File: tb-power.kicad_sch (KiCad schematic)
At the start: 56 parts, among them Q1 BC817-25W, U4 JHL6340SLLSQ

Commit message: Run kmake loclib
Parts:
- C51, C52, C53, C54, C55, C56, C57, C58, C59, C60, C61, C62, C63, C64, C65, C66, C67, C68, C69, C71, C72, C73, C74, C77, C81, C84, C85, C87, C90, C94: footprint antmicro-footprints:C_0402_1005Metric -> thunderbolt-adapter-footprints:C_0402_1005Metric; symbol antmicroCapacitors0402:C_1u_0402 -> thunderbolt-adapter:C_1u_0402
- C70, C75, C76, C78, C80, C83, C96: footprint antmicro-footprints:C_0402_1005Metric -> thunderbolt-adapter-footprints:C_0402_1005Metric; symbol antmicroCapacitors0402:C_10u_0402 -> thunderbolt-adapter:C_10u_0402
- C79, C82, C86, C89: footprint antmicro-footprints:C_0603_1608Metric -> thunderbolt-adapter-footprints:C_0603_1608Metric; symbol antmicroCapacitors0603:C_22u_0603 -> thunderbolt-adapter:C_22u_0603
- C88, C91, C92, C93, C95, C97: footprint antmicro-footprints:C_0402_1005Metric -> thunderbolt-adapter-footprints:C_0402_1005Metric; symbol antmicroCapacitors0402:C_100n_0402 -> thunderbolt-adapter:C_100n_0402
- D4: footprint antmicro-footprints:LED_0603_1608Metric_G -> thunderbolt-adapter-footprints:LED_0603_1608Metric_G; symbol antmicroLEDIndicationDiscrete:LED_G_0603_KP-1608CGCK -> thunderbolt-adapter:LED_G_0603_KP-1608CGCK
- L3: footprint antmicro-footprints:L_Vishay-IHLP1616BZ -> thunderbolt-adapter-footprints:L_Vishay-IHLP1616BZ; symbol antmicroFixedInductors:L_680n_7.6A_IHLP1616BZ -> thunderbolt-adapter:L_680n_7.6A_IHLP1616BZ
- L4: footprint antmicro-footprints:L_0603_1608Metric -> thunderbolt-adapter-footprints:L_0603_1608Metric; symbol antmicroFixedInductors:L_1u_1.8A_0603 -> thunderbolt-adapter:L_1u_1.8A_0603
- Q1: footprint antmicro-footprints:SOT-323 -> thunderbolt-adapter-footprints:SOT-323; symbol antmicroTransistorsBipolarSingle:BC817-25W -> thunderbolt-adapter:BC817-25W
- R47: footprint antmicro-footprints:R_0402_1005Metric -> thunderbolt-adapter-footprints:R_0402_1005Metric; symbol antmicroResistors0402:R_1k_0402 -> thunderbolt-adapter:R_1k_0402
- R48: footprint antmicro-footprints:R_0402_1005Metric -> thunderbolt-adapter-footprints:R_0402_1005Metric; symbol antmicroResistors0402:R_100k_0402 -> thunderbolt-adapter:R_100k_0402
- R49: footprint antmicro-footprints:R_0402_1005Metric -> thunderbolt-adapter-footprints:R_0402_1005Metric; symbol antmicroResistors0402:R_330R_0402 -> thunderbolt-adapter:R_330R_0402
- TP9: footprint antmicro-footprints:Testpoint_smd_1mm -> thunderbolt-adapter-footprints:Testpoint_smd_1mm; symbol antmicroTestPoints:TP_1mm_SMD -> thunderbolt-adapter:TP_1mm_SMD
- U4: footprint antmicro-footprints:JHL6340SLLSQ -> thunderbolt-adapter-footprints:JHL6340SLLSQ; symbol antmicroInterfaceControllers:JHL6340SLLSQ -> thunderbolt-adapter:JHL6340SLLSQ

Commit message: Rename project to thunderbolt-gpu-adapter
Fix Amphenol 10146070-113Y0LF footprint
Add missing 3D models, update selected footprints
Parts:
- C51, C52, C53, C54, C55, C56, C57, C58, C59, C60, C61, C62, C63, C64, C65, C66, C67, C68, C69, C71, C72, C73, C74, C77, C81, C84, C85, C87, C90, C94: footprint thunderbolt-adapter-footprints:C_0402_1005Metric -> thunderbolt-gpu-adapter-footprints:C_0402_1005Metric; symbol thunderbolt-adapter:C_1u_0402 -> thunderbolt-gpu-adapter:C_1u_0402
- C70, C75, C76, C78, C80, C83, C96: footprint thunderbolt-adapter-footprints:C_0402_1005Metric -> thunderbolt-gpu-adapter-footprints:C_0402_1005Metric; symbol thunderbolt-adapter:C_10u_0402 -> thunderbolt-gpu-adapter:C_10u_0402
- C79, C82, C86, C89: footprint thunderbolt-adapter-footprints:C_0603_1608Metric -> thunderbolt-gpu-adapter-footprints:C_0603_1608Metric; symbol thunderbolt-adapter:C_22u_0603 -> thunderbolt-gpu-adapter:C_22u_0603
- C88, C91, C92, C93, C95, C97: footprint thunderbolt-adapter-footprints:C_0402_1005Metric -> thunderbolt-gpu-adapter-footprints:C_0402_1005Metric; symbol thunderbolt-adapter:C_100n_0402 -> thunderbolt-gpu-adapter:C_100n_0402
- D4: footprint thunderbolt-adapter-footprints:LED_0603_1608Metric_G -> thunderbolt-gpu-adapter-footprints:LED_0603_1608Metric_G; symbol thunderbolt-adapter:LED_G_0603_KP-1608CGCK -> thunderbolt-gpu-adapter:LED_G_0603_KP-1608CGCK
- L3: footprint thunderbolt-adapter-footprints:L_Vishay-IHLP1616BZ -> thunderbolt-gpu-adapter-footprints:L_Vishay-IHLP1616BZ; symbol thunderbolt-adapter:L_680n_7.6A_IHLP1616BZ -> thunderbolt-gpu-adapter:L_680n_7.6A_IHLP1616BZ
- L4: footprint thunderbolt-adapter-footprints:L_0603_1608Metric -> thunderbolt-gpu-adapter-footprints:L_0603_1608Metric; symbol thunderbolt-adapter:L_1u_1.8A_0603 -> thunderbolt-gpu-adapter:L_1u_1.8A_0603
- Q1: footprint thunderbolt-adapter-footprints:SOT-323 -> thunderbolt-gpu-adapter-footprints:SOT-323; symbol thunderbolt-adapter:BC817-25W -> thunderbolt-gpu-adapter:BC817-25W
- R47: footprint thunderbolt-adapter-footprints:R_0402_1005Metric -> thunderbolt-gpu-adapter-footprints:R_0402_1005Metric; symbol thunderbolt-adapter:R_1k_0402 -> thunderbolt-gpu-adapter:R_1k_0402
- R48: footprint thunderbolt-adapter-footprints:R_0402_1005Metric -> thunderbolt-gpu-adapter-footprints:R_0402_1005Metric; symbol thunderbolt-adapter:R_100k_0402 -> thunderbolt-gpu-adapter:R_100k_0402
- R49: footprint thunderbolt-adapter-footprints:R_0402_1005Metric -> thunderbolt-gpu-adapter-footprints:R_0402_1005Metric; symbol thunderbolt-adapter:R_330R_0402 -> thunderbolt-gpu-adapter:R_330R_0402
- TP9: footprint thunderbolt-adapter-footprints:Testpoint_smd_1mm -> thunderbolt-gpu-adapter-footprints:Testpoint_smd_1mm; symbol thunderbolt-adapter:TP_1mm_SMD -> thunderbolt-gpu-adapter:TP_1mm_SMD
- U4: footprint thunderbolt-adapter-footprints:JHL6340SLLSQ -> thunderbolt-gpu-adapter-footprints:JHL6340SLLSQ; symbol thunderbolt-adapter:JHL6340SLLSQ -> thunderbolt-gpu-adapter:JHL6340SLLSQ

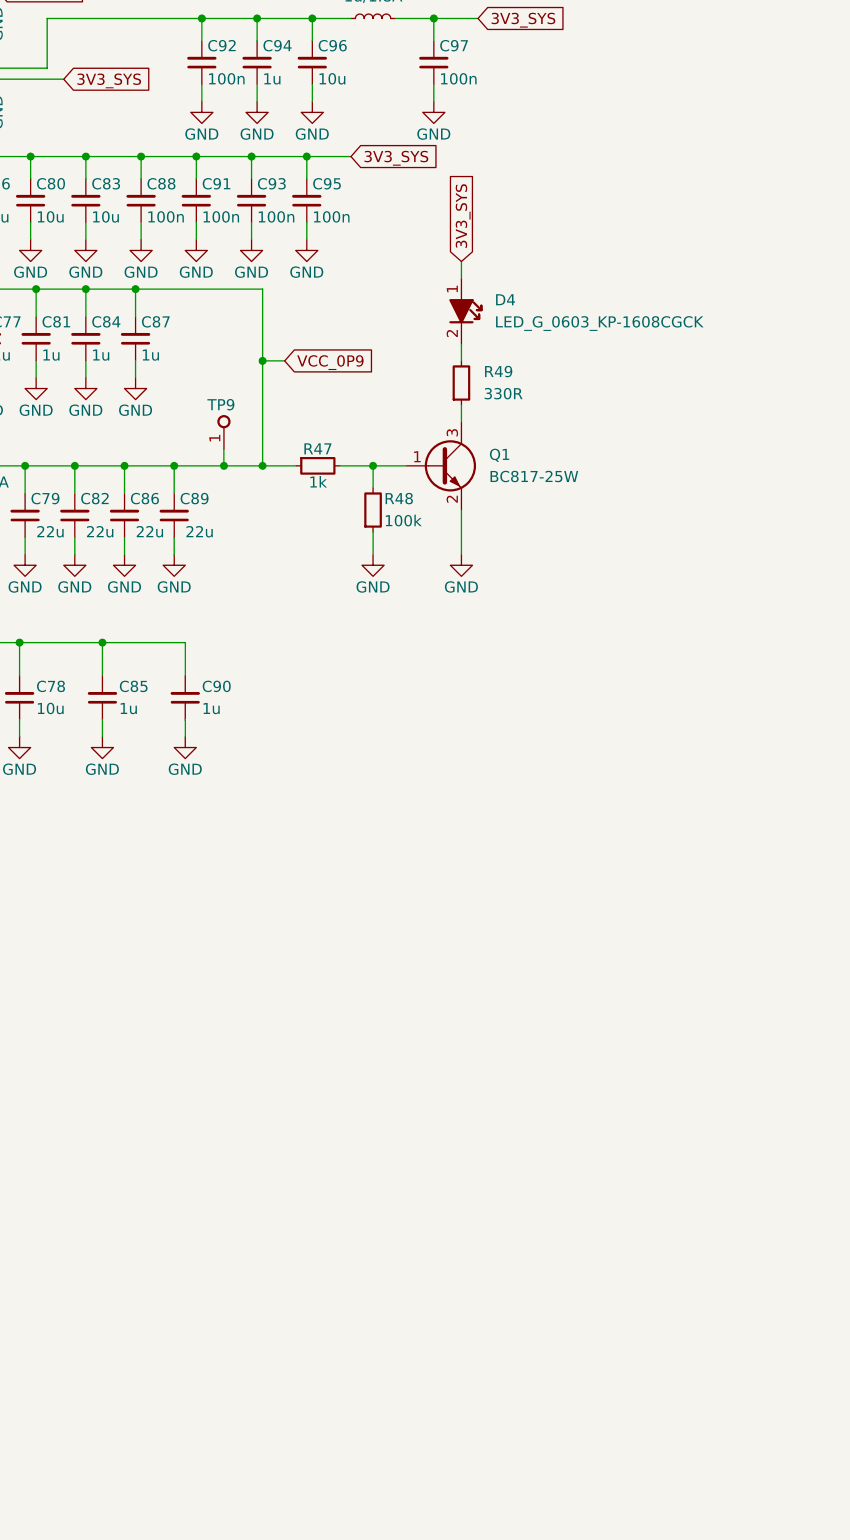
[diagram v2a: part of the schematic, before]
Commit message: Update PCIe power switching circuit (SCH)
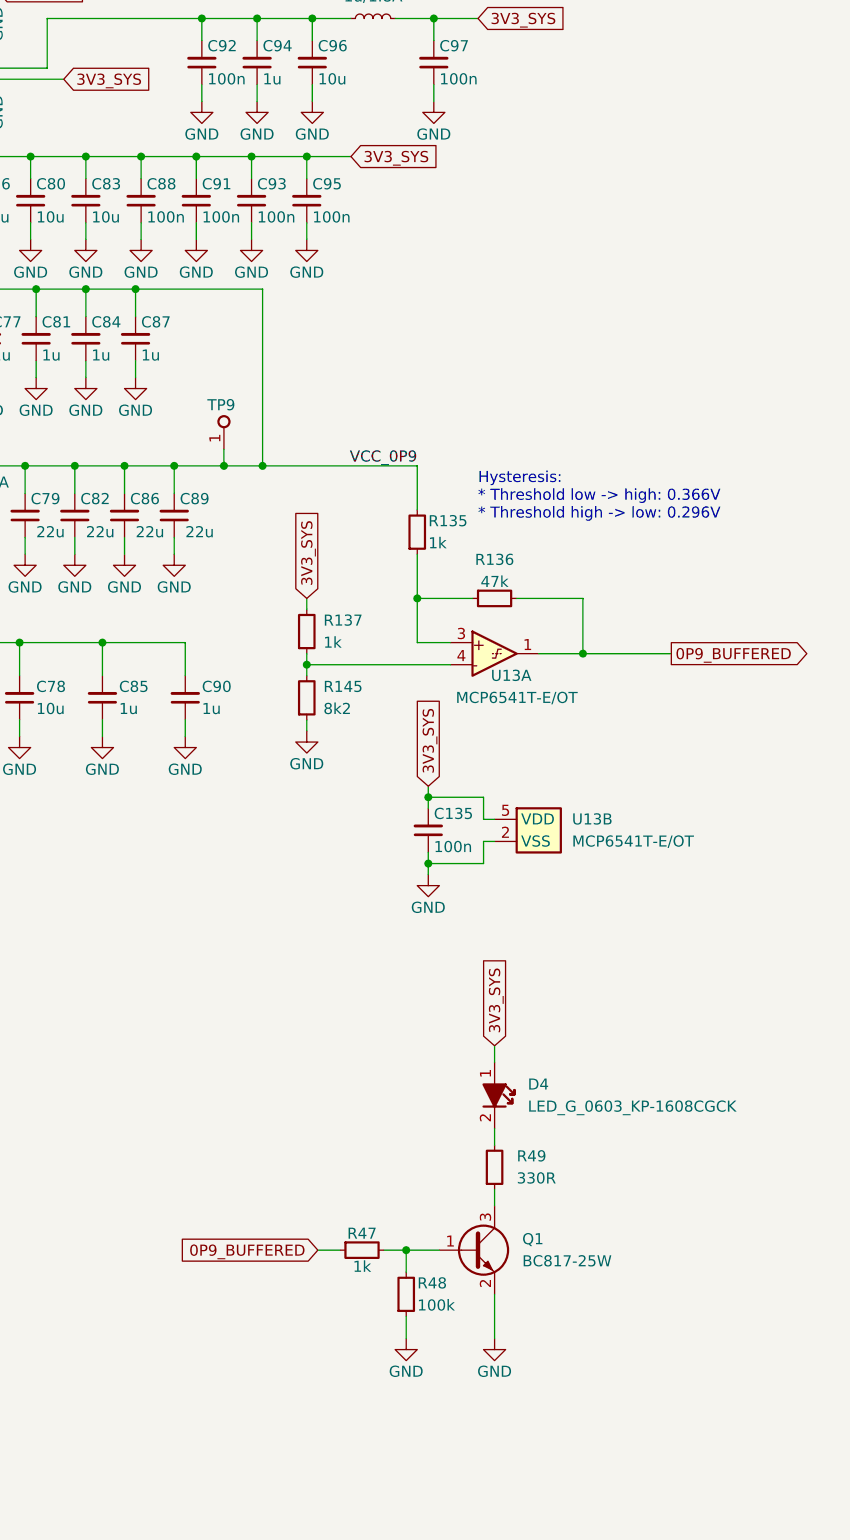
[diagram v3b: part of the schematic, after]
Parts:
- added C135: C_100n_0402, thunderbolt-gpu-adapter-footprints:C_0402_1005Metric, symbol thunderbolt-gpu-adapter:C_100n_0402
- added R135, R137: R_1k_0402, antmicro-footprints:R_0402_1005Metric, symbol antmicroResistors0402:R_1k_0402
- added R136: R_47k_0402, antmicro-footprints:R_0402_1005Metric, symbol antmicroResistors0402:R_47k_0402
- added R145: R_8k2_0402, antmicro-footprints:R_0402_1005Metric, symbol antmicroResistors0402:R_8k2_0402
- added U13: MCP6541_SOT23-5_Split, antmicro-footprints:SOT-23-5, symbol antmicroOperationalAmplifiers:MCP6541_SOT23-5_Split
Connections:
- net 3V3_SYS: now also C135.2, R137.2, U13.5 (VDD)
- net GND: now also C135.1, R145.1, U13.2 (VSS)
- net VCC_0P9: now also R135.2; no longer R47.1
- new net: R135.1, R136.1, U13.3
- new net: R137.1, R145.2, U13.4
- new net 0P9_BUFFERED: R136.2, R47.1, U13.1
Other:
- note added: "Hysteresis: * Threshold low -> high: 0.366V * Threshold high -> low: 0.296V"
- moved on the sheet: D4, Q1, R47, R48, R49

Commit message: Fix PCIe power switch - layout, bump revision to 1.1.2
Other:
- company: (none) -> Antmicro Ltd
- title: (none) -> Thunderbolt GPU Adapter
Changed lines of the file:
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@@
   (paper "A3" portrait)
   (title_block
-    (date "2023-05-09")
-    (rev "1.1.1")
+    (title "Thunderbolt GPU Adapter")
+    (date "2023-11-21")
+    (rev "1.1.2")
+    (company "Antmicro Ltd")
     (comment 1 "www.antmicro.com")
-    (comment 2 "Antmicro Ltd.")
   )
   (junction (at 116.205 80.01) (diameter 0) (color 0 0 0 0)

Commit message: Run kmake loclib
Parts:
- R135, R137: footprint antmicro-footprints:R_0402_1005Metric -> thunderbolt-gpu-adapter-footprints:R_0402_1005Metric; symbol antmicroResistors0402:R_1k_0402 -> thunderbolt-gpu-adapter:R_1k_0402
- R136: footprint antmicro-footprints:R_0402_1005Metric -> thunderbolt-gpu-adapter-footprints:R_0402_1005Metric; symbol antmicroResistors0402:R_47k_0402 -> thunderbolt-gpu-adapter:R_47k_0402
- R145: footprint antmicro-footprints:R_0402_1005Metric -> thunderbolt-gpu-adapter-footprints:R_0402_1005Metric; symbol antmicroResistors0402:R_8k2_0402 -> thunderbolt-gpu-adapter:R_8k2_0402
- U13: footprint antmicro-footprints:SOT-23-5 -> thunderbolt-gpu-adapter-footprints:SOT-23-5; symbol antmicroOperationalAmplifiers:MCP6541_SOT23-5_Split -> thunderbolt-gpu-adapter:MCP6541_SOT23-5_Split

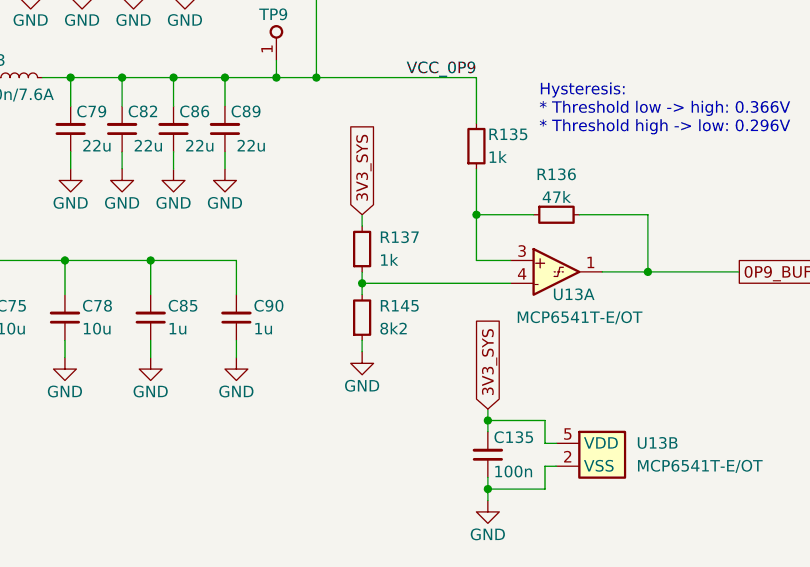
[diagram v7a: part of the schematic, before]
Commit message: Fix U13 Vref divider
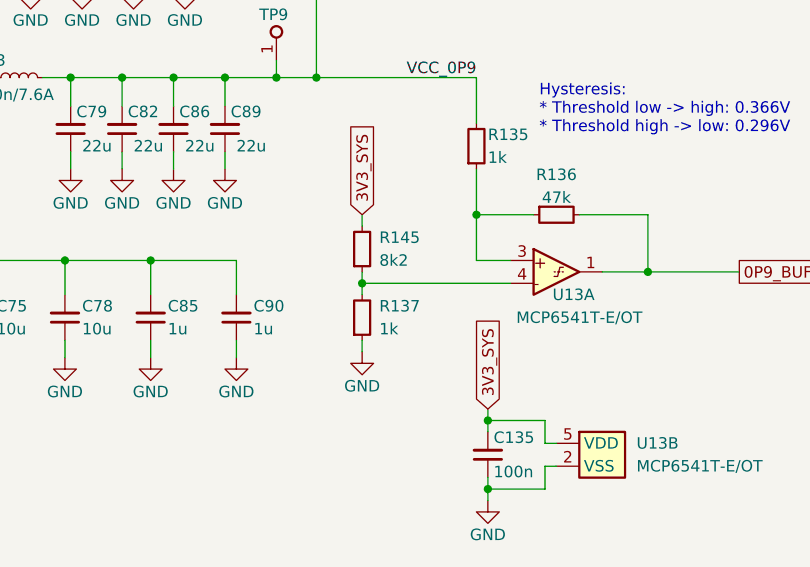
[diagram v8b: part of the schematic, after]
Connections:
- net 3V3_SYS: now also R145.2; no longer R137.2
- net GND: now also R137.1; no longer R145.1
- new net: R137.2, R145.1, U13.4
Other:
- moved on the sheet: R137, R145
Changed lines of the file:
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@@
     (pin "1")
   )
-  (symbol (lib_id "thunderbolt-gpu-adapter:R_1k_0402") (at 223.52 147.32 90) (unit 1)
-    (in_bom yes) (on_board yes)
-    (property "Reference" "R137" (id 0) (at 225.425 143.51 90)
-      (effects (font (size 1.27 1.27) (thickness 0.15)) (justify right))
-    )
-    (property "Value" "R_1k_0402" (id 1) (at 236.22 127 0)
-      (effects (font (size 1.27 1.27) (thickness 0.15)) (justify left bottom) hide)
-    )
-    (property "Footprint" "thunderbolt-gpu-adapter-footprints:R_0402_1005Metric" (id 2) (at 238.76 127 0)
-      (effects (font (size 1.27 1.27) (thickness 0.15)) (justify left bottom) hide)
-    )
-    (property "Datasheet" "https://www.bourns.com/docs/product-datasheets/cr.pdf" (id 3) (at 241.3 127 0)
-      (effects (font (size 1.27 1.27) (thickness 0.15)) (justify left bottom) hide)
-    )
-    (property "MPN" "CR0402-FX-1001GLF" (id 4) (at 243.84 127 0)
-      (effects (font (size 1.27 1.27) (thickness 0.15)) (justify left bottom) hide)
-    )
-    (property "Manufacturer" "Bourns" (id 5) (at 246.38 127 0)
-      (effects (font (size 1.27 1.27) (thickness 0.15)) (justify left bottom) hide)
-    )
-    (property "License" "Apache-2.0" (id 6) (at 248.92 127 0)
-      (effects (font (size 1.27 1.27) (thickness 0.15)) (justify left bottom) hide)
-    )
-    (property "Author" "Antmicro" (id 7) (at 251.46 127 0)
-      (effects (font (size 1.27 1.27) (thickness 0.15)) (justify left bottom) hide)
-    )
-    (property "Val" "1k" (id 8) (at 225.425 146.05 90)
-      (effects (font (size 1.27 1.27) (thickness 0.15)) (justify right))
-    )
-    (property "Tolerance" "1%" (id 9) (at 233.68 127 0)
+  (symbol (lib_id "thunderbolt-gpu-adapter:R_1k_0402") (at 223.52 154.94 90) (unit 1)
+    (in_bom yes) (on_board yes)
+    (property "Reference" "R137" (id 0) (at 225.425 151.13 90)
+      (effects (font (size 1.27 1.27) (thickness 0.15)) (justify right))
+    )
+    (property "Value" "R_1k_0402" (id 1) (at 236.22 134.62 0)
+      (effects (font (size 1.27 1.27) (thickness 0.15)) (justify left bottom) hide)
+    )
+    (property "Footprint" "thunderbolt-gpu-adapter-footprints:R_0402_1005Metric" (id 2) (at 238.76 134.62 0)
+      (effects (font (size 1.27 1.27) (thickness 0.15)) (justify left bottom) hide)
+    )
+    (property "Datasheet" "https://www.bourns.com/docs/product-datasheets/cr.pdf" (id 3) (at 241.3 134.62 0)
+      (effects (font (size 1.27 1.27) (thickness 0.15)) (justify left bottom) hide)
+    )
+    (property "MPN" "CR0402-FX-1001GLF" (id 4) (at 243.84 134.62 0)
+      (effects (font (size 1.27 1.27) (thickness 0.15)) (justify left bottom) hide)
+    )
+    (property "Manufacturer" "Bourns" (id 5) (at 246.38 134.62 0)
+      (effects (font (size 1.27 1.27) (thickness 0.15)) (justify left bottom) hide)
+    )
+    (property "License" "Apache-2.0" (id 6) (at 248.92 134.62 0)
+      (effects (font (size 1.27 1.27) (thickness 0.15)) (justify left bottom) hide)
+    )
+    (property "Author" "Antmicro" (id 7) (at 251.46 134.62 0)
+      (effects (font (size 1.27 1.27) (thickness 0.15)) (justify left bottom) hide)
+    )
+    (property "Val" "1k" (id 8) (at 225.425 153.67 90)
+      (effects (font (size 1.27 1.27) (thickness 0.15)) (justify right))
+    )
+    (property "Tolerance" "1%" (id 9) (at 233.68 134.62 0)
       (effects (font (size 1.27 1.27)) (justify left bottom) hide)
     )
@@
     (pin "2")
   )
-  (symbol (lib_id "thunderbolt-gpu-adapter:R_8k2_0402") (at 223.52 154.94 90) (unit 1)
-    (in_bom yes) (on_board yes)
-    (property "Reference" "R145" (id 0) (at 225.425 151.13 90)
-      (effects (font (size 1.27 1.27) (thickness 0.15)) (justify right))
-    )
-    (property "Value" "R_8k2_0402" (id 1) (at 236.22 134.62 0)
-      (effects (font (size 1.27 1.27) (thickness 0.15)) (justify left bottom) hide)
-    )
-    (property "Footprint" "thunderbolt-gpu-adapter-footprints:R_0402_1005Metric" (id 2) (at 238.76 134.62 0)
-      (effects (font (size 1.27 1.27) (thickness 0.15)) (justify left bottom) hide)
-    )
-    (property "Datasheet" "https://www.bourns.com/docs/product-datasheets/cr.pdf" (id 3) (at 241.3 134.62 0)
-      (effects (font (size 1.27 1.27) (thickness 0.15)) (justify left bottom) hide)
-    )
-    (property "MPN" "CR0402-FX-8201GLF" (id 4) (at 243.84 134.62 0)
-      (effects (font (size 1.27 1.27) (thickness 0.15)) (justify left bottom) hide)
-    )
-    (property "Manufacturer" "Bourns" (id 5) (at 246.38 134.62 0)
-      (effects (font (size 1.27 1.27) (thickness 0.15)) (justify left bottom) hide)
-    )
-    (property "License" "Apache-2.0" (id 6) (at 248.92 134.62 0)
-      (effects (font (size 1.27 1.27) (thickness 0.15)) (justify left bottom) hide)
-    )
-    (property "Author" "Antmicro" (id 7) (at 251.46 134.62 0)
-      (effects (font (size 1.27 1.27) (thickness 0.15)) (justify left bottom) hide)
-    )
-    (property "Val" "8k2" (id 8) (at 225.425 153.67 90)
-      (effects (font (size 1.27 1.27) (thickness 0.15)) (justify right))
-    )
-    (property "Tolerance" "1%" (id 9) (at 233.68 134.62 0)
-      (effects (font (size 1.27 1.27)) (justify left bottom) hide)
-    )
+  (symbol (lib_id "thunderbolt-gpu-adapter:R_8k2_0402") (at 223.52 147.32 90) (unit 1)
+    (in_bom yes) (on_board yes)
+    (property "Reference" "R145" (id 0) (at 225.425 143.51 90)
+      (effects (font (size 1.27 1.27) (thickness 0.15)) (justify right))
+    )
+    (property "Value" "R_8k2_0402" (id 1) (at 236.22 127 0)
+      (effects (font (size 1.27 1.27) (thickness 0.15)) (justify left bottom) hide)
+    )
+    (property "Footprint" "thunderbolt-gpu-adapter-footprints:R_0402_1005Metric" (id 2) (at 238.76 127 0)
+      (effects (font (size 1.27 1.27) (thickness 0.15)) (justify left bottom) hide)
+    )
+    (property "Datasheet" "https://www.bourns.com/docs/product-datasheets/cr.pdf" (id 3) (at 241.3 127 0)
+      (effects (font (size 1.27 1.27) (thickness 0.15)) (justify left bottom) hide)
+    )
+    (property "MPN" "CR0402-FX-8201GLF" (id 4) (at 243.84 127 0)
+      (effects (font (size 1.27 1.27) (thickness 0.15)) (justify left bottom) hide)
+    )
+    (property "Manufacturer" "Bourns" (id 5) (at 246.38 127 0)
+      (effects (font (size 1.27 1.27) (thickness 0.15)) (justify left bottom) hide)
+    )
+    (property "License" "Apache-2.0" (id 6) (at 248.92 127 0)
+      (effects (font (size 1.27 1.27) (thickness 0.15)) (justify left bottom) hide)
+    )
+    (property "Author" "Antmicro" (id 7) (at 251.46 127 0)
+      (effects (font (size 1.27 1.27) (thickness 0.15)) (justify left bottom) hide)
+    )
+    (property "Val" "8k2" (id 8) (at 225.425 146.05 90)
+      (effects (font (size 1.27 1.27) (thickness 0.15)) (justify right))
+    )
+    (property "Tolerance" "1%" (id 9) (at 233.68 127 0)
+      (effects (font (size 1.27 1.27)) (justify left bottom) hide)
+    )
